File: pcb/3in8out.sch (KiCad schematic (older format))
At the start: 15 parts, among them Q6 CSC388A, Q7 CSC388A, Q8 CSC388A, U4 74HC00, U5 74HC00, U6 74HC00

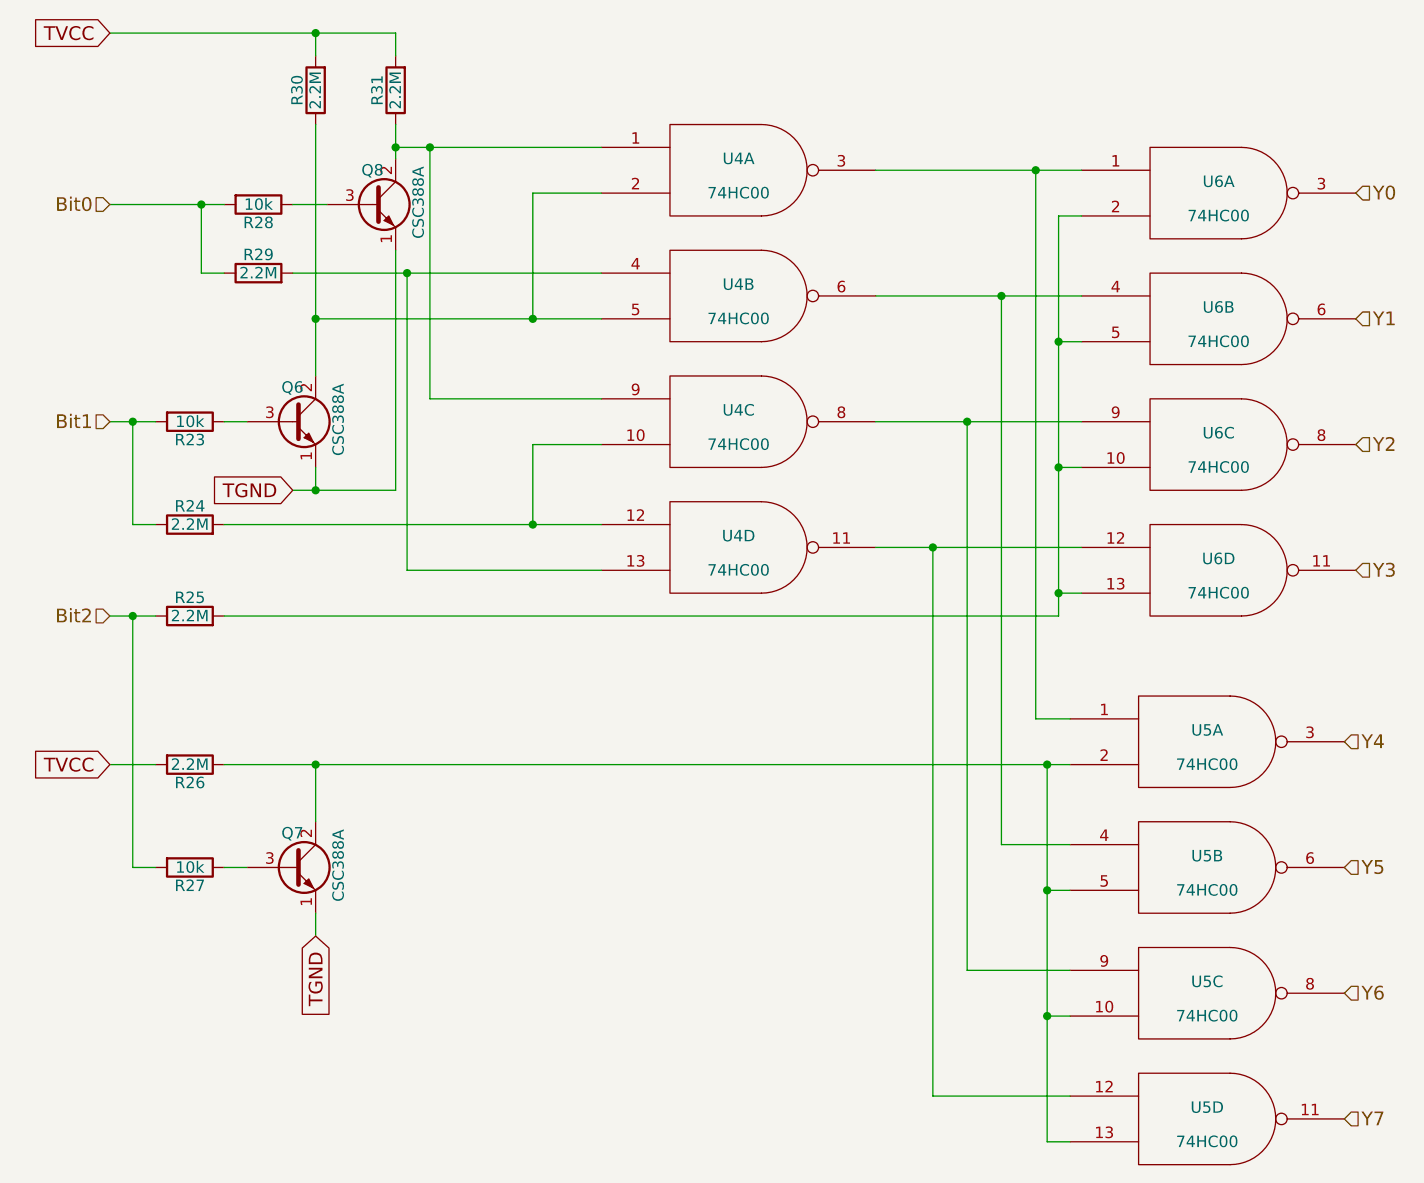
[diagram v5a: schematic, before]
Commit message: 2SC1815 のfootprintを，足の感覚が0.1inchであるfootprintに変更。
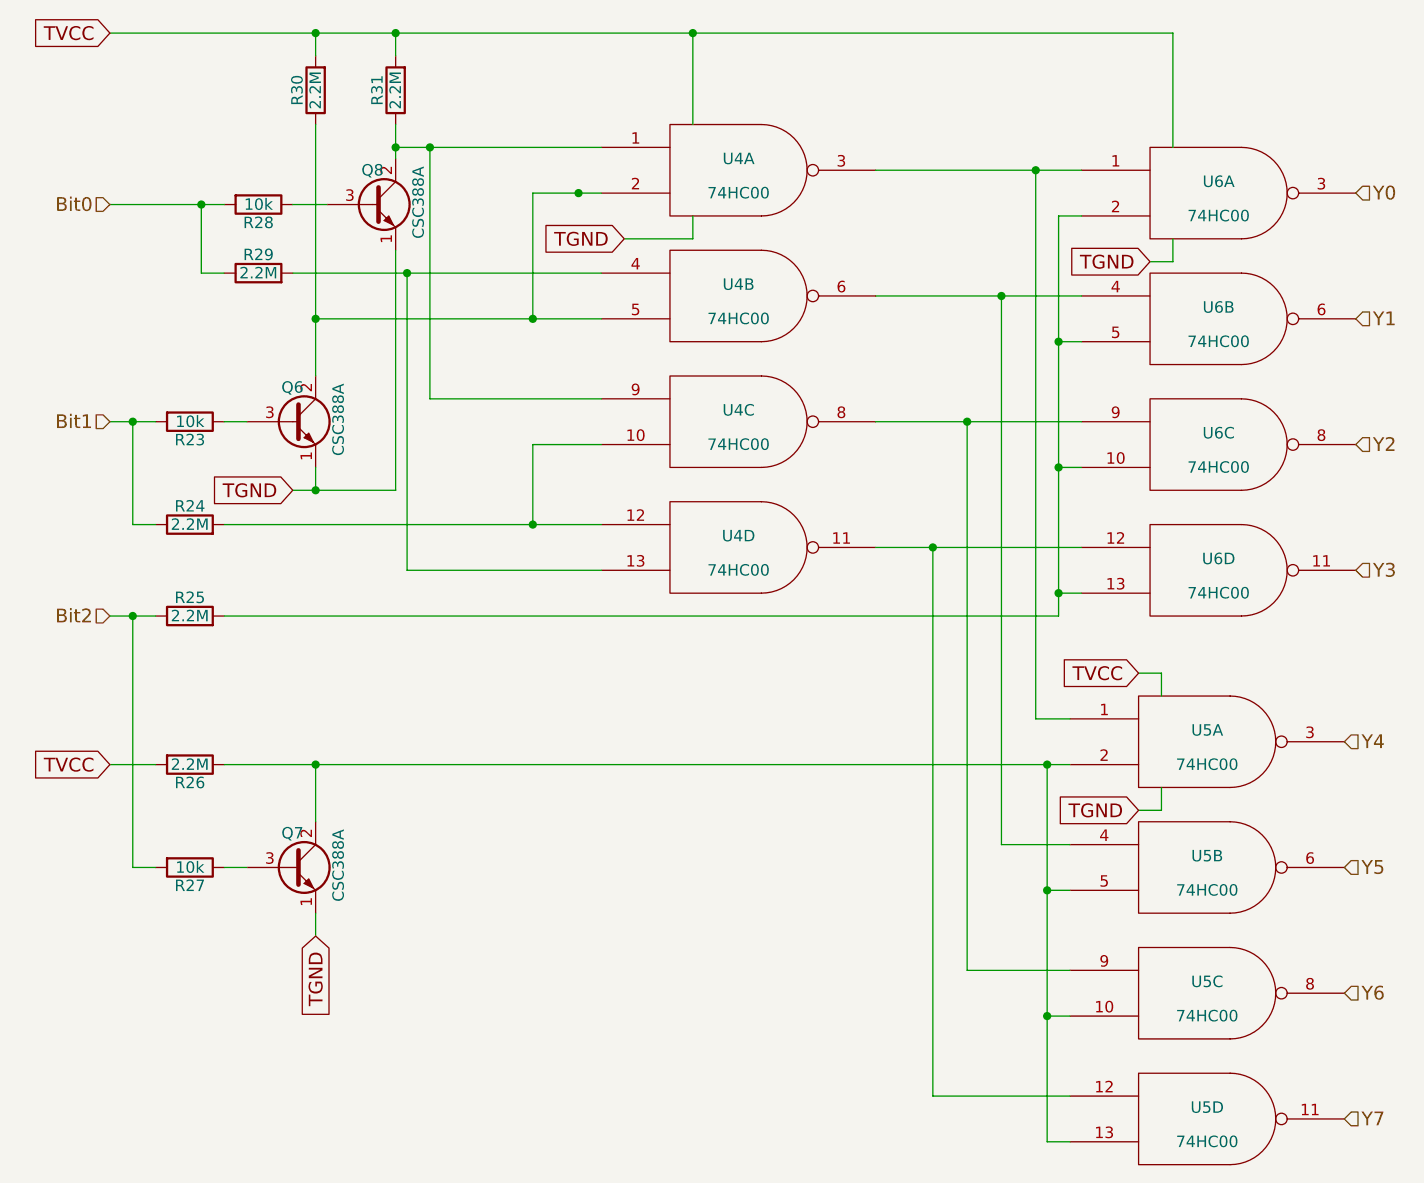
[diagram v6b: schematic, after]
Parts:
- Q6, Q7, Q8: footprint TO_SOT_Packages_THT:TO-92_Molded_Narrow -> TO_SOT_Packages_THT:TO-92_Inline_Wide
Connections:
- net TGND is gone; now on net GND_T1: Q6.1 (E), Q7.1 (E), Q8.1 (E)
- net TVCC is gone; now on net VCC_T1: R26.2, R30.2, R31.2
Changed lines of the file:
@@
 F 0 "Q8" H 3700 1950 50  0000 L CNN
 F 1 "CSC388A" V 3950 1650 50  0000 L CNN
-F 2 "TO_SOT_Packages_THT:TO-92_Molded_Narrow" H 3950 1725 50  0001 L CIN
+F 2 "TO_SOT_Packages_THT:TO-92_Inline_Wide" H 3950 1725 50  0001 L CIN
 F 3 "" H 3750 1800 50  0001 L CNN
 	1    3750 1800
@@
 F 0 "Q6" H 3350 2900 50  0000 L CNN
 F 1 "CSC388A" V 3600 2600 50  0000 L CNN
-F 2 "TO_SOT_Packages_THT:TO-92_Molded_Narrow" H 3600 2675 50  0001 L CIN
+F 2 "TO_SOT_Packages_THT:TO-92_Inline_Wide" H 3600 2675 50  0001 L CIN
 F 3 "" H 3400 2750 50  0001 L CNN
 	1    3400 2750
@@
 	0    -1   -1   0
 $EndComp
-Wire Wire Line
-	3400 1800 3550 1800
-Wire Wire Line
-	3850 1450 3850 1600
-Wire Wire Line
-	3100 2100 3000 2100
-Wire Wire Line
-	3000 2100 3000 1800
-Wire Wire Line
-	2600 1800 3100 1800
-Connection ~ 3000 1800
-Wire Wire Line
-	3400 2100 4750 2100
-Wire Wire Line
-	3850 1550 4750 1550
-Connection ~ 3850 1550
-Wire Wire Line
-	4750 2650 4000 2650
-Wire Wire Line
-	4000 2650 4000 1550
-Connection ~ 4000 1550
-Wire Wire Line
-	3900 2100 3900 3400
-Wire Wire Line
-	3900 3400 4750 3400
-Connection ~ 3900 2100
-Wire Wire Line
-	3100 2750 3200 2750
-Wire Wire Line
-	3500 1450 3500 2550
-Wire Wire Line
-	2800 3200 2700 3200
-Wire Wire Line
-	2700 3200 2700 2750
-Wire Wire Line
-	2600 2750 2800 2750
-Connection ~ 2700 2750
-Wire Wire Line
-	3500 2950 3500 3050
-Wire Wire Line
-	3100 3200 4750 3200
-Wire Wire Line
-	3500 2300 4750 2300
-Connection ~ 3500 2300
-Wire Wire Line
-	4450 2300 4450 1750
-Wire Wire Line
-	4450 1750 4750 1750
-Connection ~ 4450 2300
-Wire Wire Line
-	4750 2850 4450 2850
-Wire Wire Line
-	4450 2850 4450 3200
-Connection ~ 4450 3200
-Wire Wire Line
-	3400 3050 3850 3050
 $Comp
 L CSC388A Q7
@@
 F 0 "Q7" H 3350 4850 50  0000 L CNN
 F 1 "CSC388A" V 3600 4550 50  0000 L CNN
-F 2 "TO_SOT_Packages_THT:TO-92_Molded_Narrow" H 3600 4625 50  0001 L CIN
+F 2 "TO_SOT_Packages_THT:TO-92_Inline_Wide" H 3600 4625 50  0001 L CIN
 F 3 "" H 3400 4700 50  0001 L CNN
 	1    3400 4700
@@
 	0    -1   -1   0
 $EndComp
-Wire Wire Line
-	3100 4700 3200 4700
-Wire Wire Line
-	3100 4250 6800 4250
-Wire Wire Line
-	3500 4250 3500 4500
-Wire Wire Line
-	2600 3600 2800 3600
-Wire Wire Line
-	2700 3600 2700 4700
-Wire Wire Line
-	2700 4700 2800 4700
-Wire Wire Line
-	3500 4900 3500 5000
-Wire Wire Line
-	6750 3600 3100 3600
 $Comp
 L R R26
@@
 	0    1    1    0
 $EndComp
-Wire Wire Line
-	5950 1650 6850 1650
-Wire Wire Line
-	6800 4050 6650 4050
-Wire Wire Line
-	6650 4050 6650 1650
-Connection ~ 6650 1650
-Wire Wire Line
-	5950 2200 6850 2200
-Wire Wire Line
-	5950 2750 6850 2750
-Wire Wire Line
-	5950 3300 6850 3300
-Wire Wire Line
-	6800 4600 6500 4600
-Wire Wire Line
-	6500 4600 6500 2200
-Connection ~ 6500 2200
-Connection ~ 2700 3600
-Wire Wire Line
-	6750 1850 6750 3600
-Wire Wire Line
-	6750 2950 6850 2950
-Wire Wire Line
-	6750 1850 6850 1850
-Connection ~ 6750 2950
-Wire Wire Line
-	6850 2400 6750 2400
-Connection ~ 6750 2400
-Wire Wire Line
-	6700 4250 6700 5900
-Wire Wire Line
-	6700 5900 6800 5900
-Wire Wire Line
-	6800 5350 6700 5350
-Connection ~ 6700 5350
-Wire Wire Line
-	6800 4800 6700 4800
-Connection ~ 6700 4800
-Connection ~ 6700 4250
-Connection ~ 3500 4250
 Text HLabel 2600 1800 0    60   Input ~ 0
 Bit0
@@
 Text HLabel 8000 5800 2    60   Input ~ 0
 Y7
+Text GLabel 2600 4250 0    60   Input ~ 0
+TVCC
+Text GLabel 3500 5000 3    60   Input ~ 0
+TGND
+Text GLabel 2600 1050 0    60   Input ~ 0
+TVCC
+Text GLabel 3400 3050 0    60   Input ~ 0
+TGND
+Wire Wire Line
+	3400 1800 3550 1800
+Wire Wire Line
+	3850 1450 3850 1600
+Wire Wire Line
+	3100 2100 3000 2100
+Wire Wire Line
+	3000 2100 3000 1800
+Wire Wire Line
+	2600 1800 3100 1800
+Connection ~ 3000 1800
+Wire Wire Line
+	3400 2100 4750 2100
+Wire Wire Line
+	3850 1550 4750 1550
+Connection ~ 3850 1550
+Wire Wire Line
+	4750 2650 4000 2650
+Wire Wire Line
+	4000 2650 4000 1550
+Connection ~ 4000 1550
+Wire Wire Line
+	3900 2100 3900 3400
+Wire Wire Line
+	3900 3400 4750 3400
+Connection ~ 3900 2100
+Wire Wire Line
+	3100 2750 3200 2750
+Wire Wire Line
+	3500 1450 3500 2550
+Wire Wire Line
+	2800 3200 2700 3200
+Wire Wire Line
+	2700 3200 2700 2750
+Wire Wire Line
+	2600 2750 2800 2750
+Connection ~ 2700 2750
+Wire Wire Line
+	3500 2950 3500 3050
+Wire Wire Line
+	3100 3200 4750 3200
+Wire Wire Line
+	3500 2300 4750 2300
+Connection ~ 3500 2300
+Wire Wire Line
+	4450 2300 4450 1750
+Wire Wire Line
+	4450 1750 4750 1750
+Connection ~ 4450 2300
+Wire Wire Line
+	4750 2850 4450 2850
+Wire Wire Line
+	4450 2850 4450 3200
+Connection ~ 4450 3200
+Wire Wire Line
+	3400 3050 3850 3050
+Wire Wire Line
+	3100 4700 3200 4700
+Wire Wire Line
+	3100 4250 6800 4250
+Wire Wire Line
+	3500 4250 3500 4500
+Wire Wire Line
+	2600 3600 2800 3600
+Wire Wire Line
+	2700 3600 2700 4700
+Wire Wire Line
+	2700 4700 2800 4700
+Wire Wire Line
+	3500 4900 3500 5000
+Wire Wire Line
+	6750 3600 3100 3600
+Wire Wire Line
+	5950 1650 6850 1650
+Wire Wire Line
+	6800 4050 6650 4050
+Wire Wire Line
+	6650 4050 6650 1650
+Connection ~ 6650 1650
+Wire Wire Line
+	5950 2200 6850 2200
+Wire Wire Line
+	5950 2750 6850 2750
+Wire Wire Line
+	5950 3300 6850 3300
+Wire Wire Line
+	6800 4600 6500 4600
+Wire Wire Line
+	6500 4600 6500 2200
+Connection ~ 6500 2200
+Connection ~ 2700 3600
+Wire Wire Line
+	6750 1850 6750 3600
+Wire Wire Line
+	6750 2950 6850 2950
+Wire Wire Line
+	6750 1850 6850 1850
+Connection ~ 6750 2950
+Wire Wire Line
+	6850 2400 6750 2400
+Connection ~ 6750 2400
+Wire Wire Line
+	6700 4250 6700 5900
+Wire Wire Line
+	6700 5900 6800 5900
+Wire Wire Line
+	6800 5350 6700 5350
+Connection ~ 6700 5350
+Wire Wire Line
+	6800 4800 6700 4800
+Connection ~ 6700 4800
+Connection ~ 6700 4250
+Connection ~ 3500 4250
 Wire Wire Line
 	6350 5150 6350 2750
@@
 	6200 5700 6200 3300
 Connection ~ 6200 3300
-Text GLabel 2600 4250 0    60   Input ~ 0
-TVCC
 Wire Wire Line
 	2600 4250 2800 4250
 Wire Wire Line
 	3850 3050 3850 2000
-Text GLabel 3500 5000 3    60   Input ~ 0
-TGND
 Wire Wire Line
 	6850 3500 6750 3500
 Connection ~ 6750 3500
-Text GLabel 2600 1050 0    60   Input ~ 0
-TVCC
-Wire Wire Line
-	2600 1050 3850 1050
+Wire Wire Line
+	2600 1050 7250 1050
 Wire Wire Line
 	3850 1050 3850 1150
@@
 	3500 1150 3500 1050
 Connection ~ 3500 1050
-Text GLabel 3400 3050 0    60   Input ~ 0
-TGND
 Connection ~ 3500 3050
 Wire Wire Line
 	6800 5700 6200 5700
+Wire Wire Line
+	5150 1050 5150 1450
+Connection ~ 3850 1050
+Connection ~ 5150 1050
+Text GLabel 7100 3850 0    60   Input ~ 0
+TVCC
+Wire Wire Line
+	7100 3850 7200 3850
+Wire Wire Line
+	7200 3850 7200 3950
+Wire Wire Line
+	5150 1950 5150 1850
+Wire Wire Line
+	4850 1950 5150 1950
+Connection ~ 4650 1750
+Wire Wire Line
+	7250 1950 7250 2050
+Wire Wire Line
+	7200 4350 7200 4450
+Text GLabel 4850 1950 0    60   Input ~ 0
+TGND
+Text GLabel 7150 2050 0    60   Input ~ 0
+TGND
+Wire Wire Line
+	7250 2050 7150 2050
+Text GLabel 7100 4450 0    60   Input ~ 0
+TGND
+Wire Wire Line
+	7200 4450 7100 4450
+Wire Wire Line
+	7250 1050 7250 1550
 $EndSCHEMATC
